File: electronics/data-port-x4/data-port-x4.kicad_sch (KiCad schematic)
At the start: 0 parts

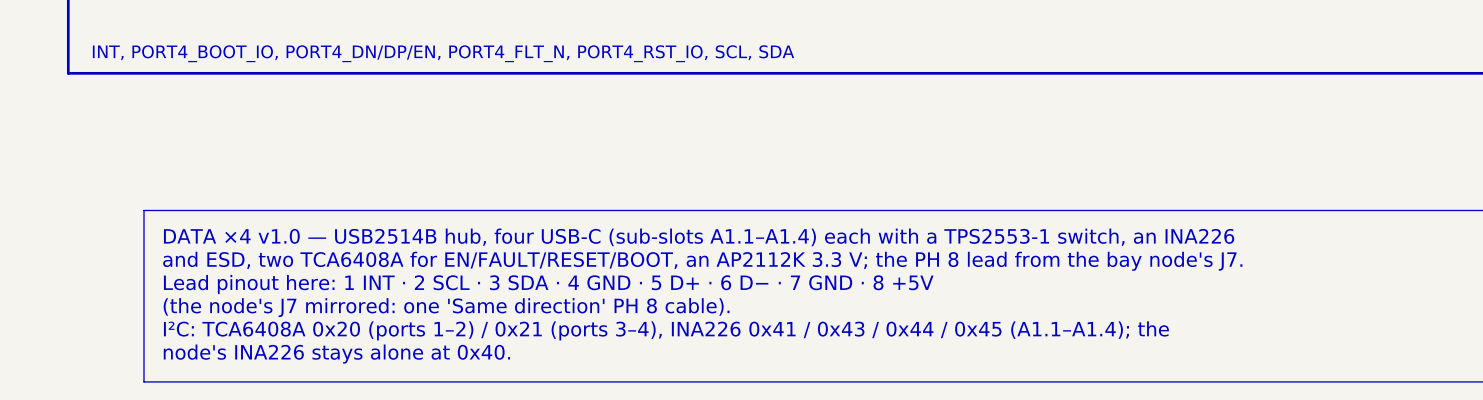
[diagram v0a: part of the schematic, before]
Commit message: DATA ×4: the lead's D+/D− follow J7, the upstream pair rerouted
The node's J7 now has D+ on pin 3 and D− on pin 4 (094341c); the lead
mirrors pins (n ↔ 9 − n), so J1 takes D− on pin 5 and D+ on pin 6, like
the single DATA port's J2.  The upstream pair is drawn again without a
crossover: two vias in front of J1 (D+ north of D−), B.Cu west, north
along x 87 (clear of In2's +3V3 edge), west and south into the hub's top
pins; every turn keeps D+ on the pair's right, west of D− at the hub.

The new route moved the router's vias, and two of them cut In2's +5V in
half under the hub's capacitors: the +3V3 tab there ends at y 21.6 and a
via-only keep-out (pcbgen keepouts "vias_only") keeps the 1.9 mm +5V neck
whole.  The 22 µF VBUS caps' LCSC/MPN fields now reach the schematic and
the PCB too.  Docs: the lead pinout row.

ERC 0, DRC 0 (unconnected 0, parity 0); Konnect: 0 errors, the same three
library-copy warnings, JLC DFM 0.

Co-Authored-By: Claude Opus 5.5 <noreply@anthropic.com>
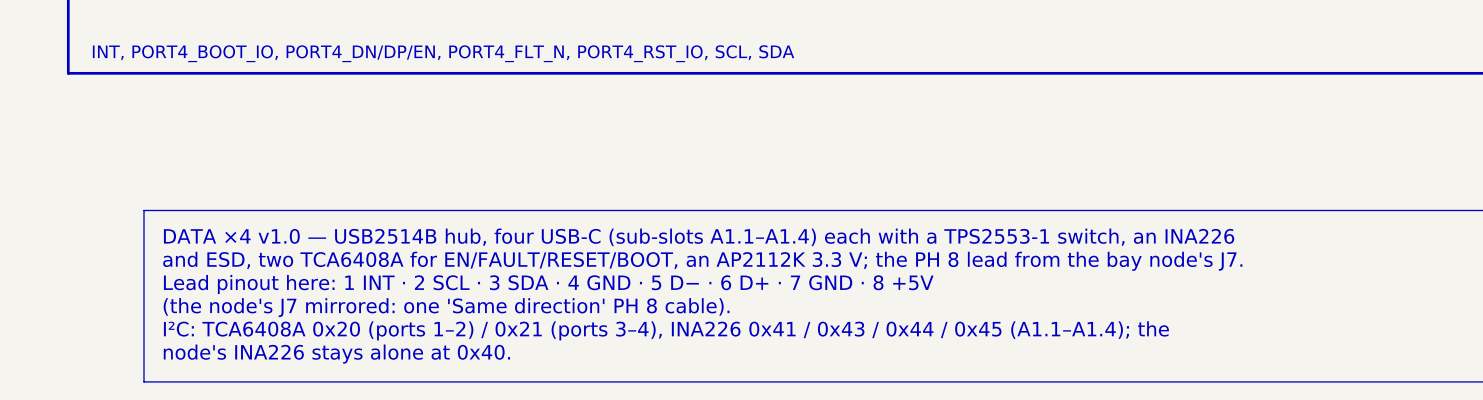
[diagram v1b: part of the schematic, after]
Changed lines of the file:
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@@
 		)
 	)
-	(text_box "DATA ×4 v1.0 — USB2514B hub, four USB-C (sub-slots A1.1–A1.4) each with a TPS2553-1 switch, an INA226\n  and ESD, two TCA6408A for EN/FAULT/RESET/BOOT, an AP2112K 3.3 V; the PH 8 lead from the bay node's J7.\nLead pinout here: 1 INT · 2 SCL · 3 SDA · 4 GND · 5 D+ · 6 D− · 7 GND · 8 +5V\n  (the node's J7 mirrored: one 'Same direction' PH 8 cable).\nI²C: TCA6408A 0x20 (ports 1–2) / 0x21 (ports 3–4), INA226 0x41 / 0x43 / 0x44 / 0x45 (A1.1–A1.4); the\n  node's INA226 stays alone at 0x40."
+	(text_box "DATA ×4 v1.0 — USB2514B hub, four USB-C (sub-slots A1.1–A1.4) each with a TPS2553-1 switch, an INA226\n  and ESD, two TCA6408A for EN/FAULT/RESET/BOOT, an AP2112K 3.3 V; the PH 8 lead from the bay node's J7.\nLead pinout here: 1 INT · 2 SCL · 3 SDA · 4 GND · 5 D− · 6 D+ · 7 GND · 8 +5V\n  (the node's J7 mirrored: one 'Same direction' PH 8 cable).\nI²C: TCA6408A 0x20 (ports 1–2) / 0x21 (ports 3–4), INA226 0x41 / 0x43 / 0x44 / 0x45 (A1.1–A1.4); the\n  node's INA226 stays alone at 0x40."
 		(exclude_from_sim no)
 		(at 30 219.71 0)

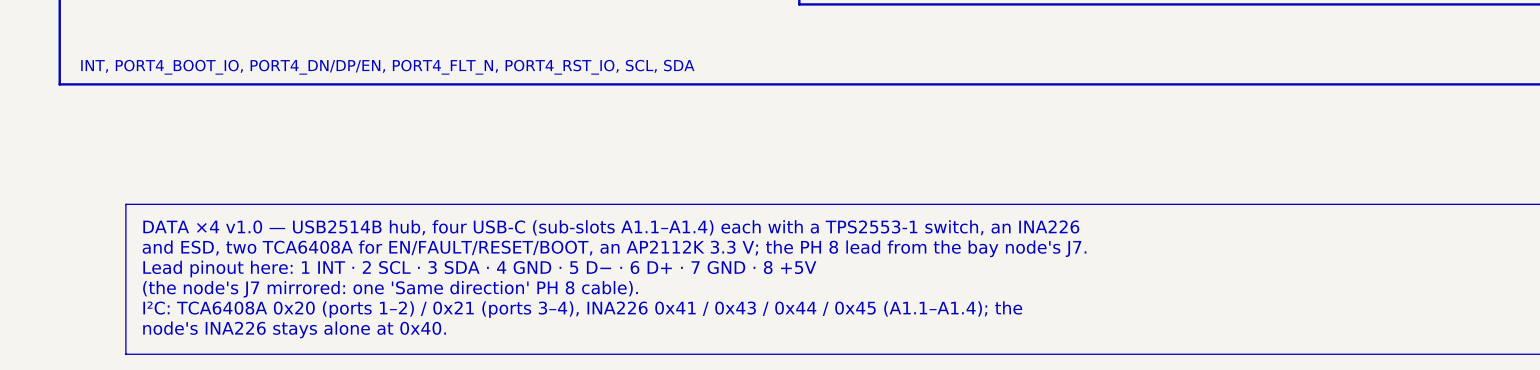
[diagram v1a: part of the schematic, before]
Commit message: DATA ×4: a basic-part LDO, the XC6206 in U3's spot
U3 goes from the AP2112K-3.3 (extended) to the XC6206P332MR-G (C5446,
JLC basic, SOT-23-3): one extended part type fewer, $3.07 an order at
Economic PCBA.  Its dropout is ≈ 0.25 V at 0.1 A against the board's
≈ 0.1 A of logic, so the hub, the expanders and the INA226s still run
down to ≈ 3.6 V in; 200 mA max, 6 V in max (the node's +5V is 5.24 V).
The AMS1117 suggested first doesn't fit (SOT-223 under J1) and its ≈ 1 V
dropout would eat the lead's margin.  U3 sits at 0° (of three
orientations routed, the one Freerouting closed), CPL fix 180° for
C5446.

Re-routed: ERC 0, DRC 0 (unconnected 0, parity 0).  BOM: the DATA ×4
quote at 8 extended types ($74.44), its lever moves out of JLC_LEVERS.

Co-Authored-By: Claude Opus 5.5 <noreply@anthropic.com>
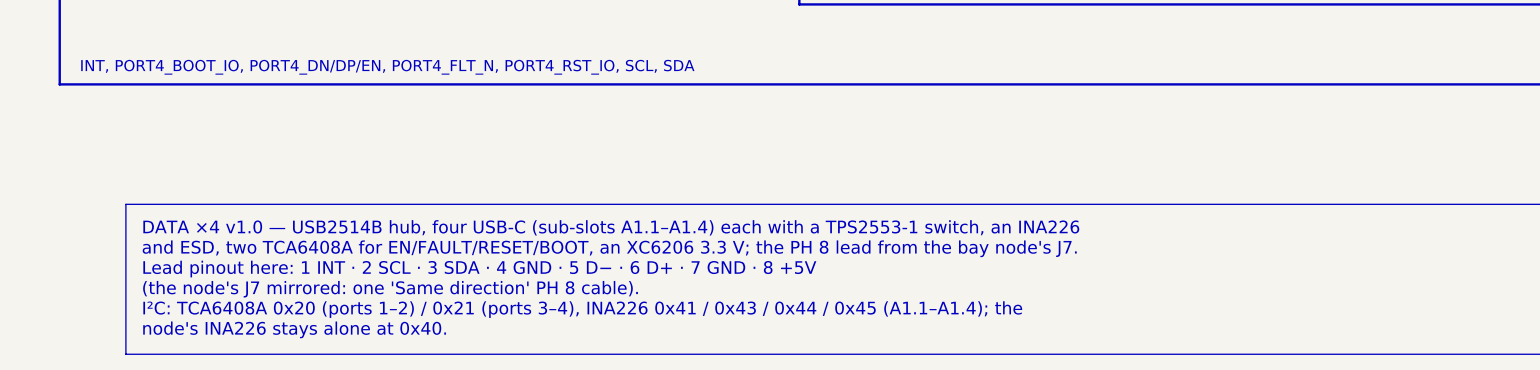
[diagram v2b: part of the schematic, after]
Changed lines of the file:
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@@
 		)
 	)
-	(text_box "DATA ×4 v1.0 — USB2514B hub, four USB-C (sub-slots A1.1–A1.4) each with a TPS2553-1 switch, an INA226\n  and ESD, two TCA6408A for EN/FAULT/RESET/BOOT, an AP2112K 3.3 V; the PH 8 lead from the bay node's J7.\nLead pinout here: 1 INT · 2 SCL · 3 SDA · 4 GND · 5 D− · 6 D+ · 7 GND · 8 +5V\n  (the node's J7 mirrored: one 'Same direction' PH 8 cable).\nI²C: TCA6408A 0x20 (ports 1–2) / 0x21 (ports 3–4), INA226 0x41 / 0x43 / 0x44 / 0x45 (A1.1–A1.4); the\n  node's INA226 stays alone at 0x40."
+	(text_box "DATA ×4 v1.0 — USB2514B hub, four USB-C (sub-slots A1.1–A1.4) each with a TPS2553-1 switch, an INA226\n  and ESD, two TCA6408A for EN/FAULT/RESET/BOOT, an XC6206 3.3 V; the PH 8 lead from the bay node's J7.\nLead pinout here: 1 INT · 2 SCL · 3 SDA · 4 GND · 5 D− · 6 D+ · 7 GND · 8 +5V\n  (the node's J7 mirrored: one 'Same direction' PH 8 cable).\nI²C: TCA6408A 0x20 (ports 1–2) / 0x21 (ports 3–4), INA226 0x41 / 0x43 / 0x44 / 0x45 (A1.1–A1.4); the\n  node's INA226 stays alone at 0x40."
 		(exclude_from_sim no)
 		(at 30 219.71 0)

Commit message: DATA ×4: back to the AP2112K on U3, on top-side copper
The XC6206 (82c7172) can't carry this rail.  The USB2514B alone draws up
to 155 mA at high speed with four ports busy (datasheet tables 6-4 and
6-5; 84 mA at full speed), so the LDO burns ≈ 0.31 W from 5.24 V: more
than a 200 mA SOT-23 LDO like the XC6206 is rated for (≈ 0.25 W), and the
XC6206 has no thermal shutdown.  The AP2112K-3.3 (600 mA, thermal
shutdown) is back on its SOT-23-5 footprint at 0°, CPL 270° as before;
C5446 and its catalog entry go.

Its VIN and EN pins (with C2's +5V pad) and its GND pin now sit on
top-side islands (exclusive, thermal reliefs) with their own vias to the
+5V and GND planes, to spread that heat.  design.py and docs/electronics.md
say why, so it isn't swapped again.

Re-routed: ERC 0, DRC 0 (unconnected 0, parity 0).  BOM: back to 9
extended types, the DATA ×4 order $103.76.

Co-Authored-By: Claude Opus 5.5 <noreply@anthropic.com>
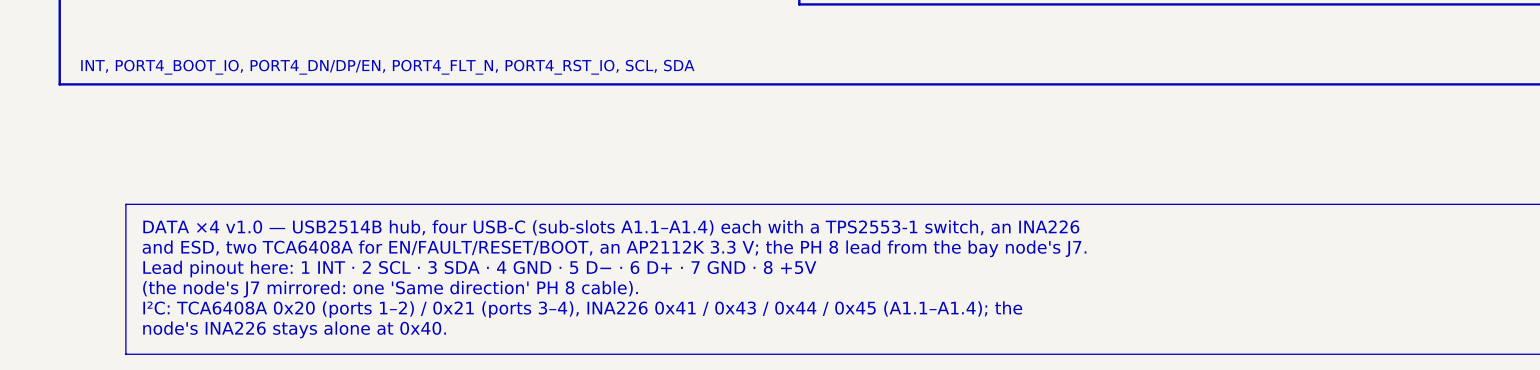
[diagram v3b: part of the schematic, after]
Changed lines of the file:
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@@
 		)
 	)
-	(text_box "DATA ×4 v1.0 — USB2514B hub, four USB-C (sub-slots A1.1–A1.4) each with a TPS2553-1 switch, an INA226\n  and ESD, two TCA6408A for EN/FAULT/RESET/BOOT, an XC6206 3.3 V; the PH 8 lead from the bay node's J7.\nLead pinout here: 1 INT · 2 SCL · 3 SDA · 4 GND · 5 D− · 6 D+ · 7 GND · 8 +5V\n  (the node's J7 mirrored: one 'Same direction' PH 8 cable).\nI²C: TCA6408A 0x20 (ports 1–2) / 0x21 (ports 3–4), INA226 0x41 / 0x43 / 0x44 / 0x45 (A1.1–A1.4); the\n  node's INA226 stays alone at 0x40."
+	(text_box "DATA ×4 v1.0 — USB2514B hub, four USB-C (sub-slots A1.1–A1.4) each with a TPS2553-1 switch, an INA226\n  and ESD, two TCA6408A for EN/FAULT/RESET/BOOT, an AP2112K 3.3 V; the PH 8 lead from the bay node's J7.\nLead pinout here: 1 INT · 2 SCL · 3 SDA · 4 GND · 5 D− · 6 D+ · 7 GND · 8 +5V\n  (the node's J7 mirrored: one 'Same direction' PH 8 cable).\nI²C: TCA6408A 0x20 (ports 1–2) / 0x21 (ports 3–4), INA226 0x41 / 0x43 / 0x44 / 0x45 (A1.1–A1.4); the\n  node's INA226 stays alone at 0x40."
 		(exclude_from_sim no)
 		(at 30 219.71 0)

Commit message: DATA ×4: 100 × 28 mm, the lead on the right edge
The board shrinks to 100 mm (JLC's 4-layer offer, no engineering fee)
and grows 4 mm towards the rear: 100 × 28, no notch.  The four USB-C,
their ports, pairs and ESD flow-through stay exactly where they were
(the layout moves 4 mm off the rear edge as a whole, DY in design.py).
J1 (PH 8, side entry) moves to the right edge, its mouth at drawer x 115,
pin 1 at the front; its lead ESDs face its pins, U4 turned 270°, U5 level
with pin 1; C1 by its +5V pin; U3 behind it, turned 180° with its VIN,
EN and GND islands (the same shapes) and a +3V3 bump in In2 under its
output.  H1-H3 keep their drawer spots, H4 moves to the rear-right corner
(96.8, 3.5): the drawer's one set of DATA ×4 bosses, the v2's too.

Routing against the 108 mm board: the upstream pair goes from 26 / 25 mm
to 15 / 15 mm, two vias each as before; the 16 port pair nets are
unchanged to 0.05 mm and to the via; no B.Cu pair segment over In2's
+3V3 (both notches kept); the +5V neck under the hub stays 2.44 mm with
no via; the LDO islands are as large (EN 4.7 mm² against 4.4).  Router
copper 721 mm and 91 vias against 799 mm and 93.  Port 3's INA226 A1
strap gets a via of its own (its fan-out had no room, Freerouting missed
it now and then).  Nothing ends up worse.

ERC 0, DRC 0, parity 0, 0 unconnected (the best of seven routing
variants on the Mac and zephyrbox).  The review's CPL audit agrees on all
106 parts.  rack.yaml carries the new size, holes and J1 (`lead`, the
notch and `ph` gone); the viewer's stand-in shows J1 on the right edge
and brings the lead up beside the board.  The bare PCB is priced at the
bay node's 4-layer offer ($13.20 for 5) until the JLC-cost owner
re-quotes it: about $85 for 5 with 2 assembled instead of $104.  The
drawer's window and the new H4 boss are the Mechanics session's.

Co-Authored-By: Claude Opus 5.5 <noreply@anthropic.com>
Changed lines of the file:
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@@
 		)
 	)
-	(text_box "DATA ×4 v1.0 — USB2514B hub, four USB-C (sub-slots A1.1–A1.4) each with a TPS2553-1 switch, an INA226\n  and ESD, two TCA6408A for EN/FAULT/RESET/BOOT, an AP2112K 3.3 V; the PH 8 lead from the bay node's J7.\nLead pinout here: 1 INT · 2 SCL · 3 SDA · 4 GND · 5 D− · 6 D+ · 7 GND · 8 +5V\n  (the node's J7 mirrored: one 'Same direction' PH 8 cable).\nI²C: TCA6408A 0x20 (ports 1–2) / 0x21 (ports 3–4), INA226 0x41 / 0x43 / 0x44 / 0x45 (A1.1–A1.4); the\n  node's INA226 stays alone at 0x40."
+	(text_box "DATA ×4 v1.0 — USB2514B hub, four USB-C (sub-slots A1.1–A1.4) each with a TPS2553-1 switch, an INA226\n  and ESD, two TCA6408A for EN/FAULT/RESET/BOOT, an AP2112K 3.3 V; the PH 8 lead from the bay node's J7\n  into J1 on the right edge.  100 × 28 mm.\nLead pinout here: 1 INT · 2 SCL · 3 SDA · 4 GND · 5 D− · 6 D+ · 7 GND · 8 +5V\n  (the node's J7 mirrored: one 'Same direction' PH 8 cable).\nI²C: TCA6408A 0x20 (ports 1–2) / 0x21 (ports 3–4), INA226 0x41 / 0x43 / 0x44 / 0x45 (A1.1–A1.4); the\n  node's INA226 stays alone at 0x40."
 		(exclude_from_sim no)
 		(at 30 219.71 0)
-		(size 360 19.05)
+		(size 360 21.59)
 		(margins 2 2 2 2)
 		(stroke

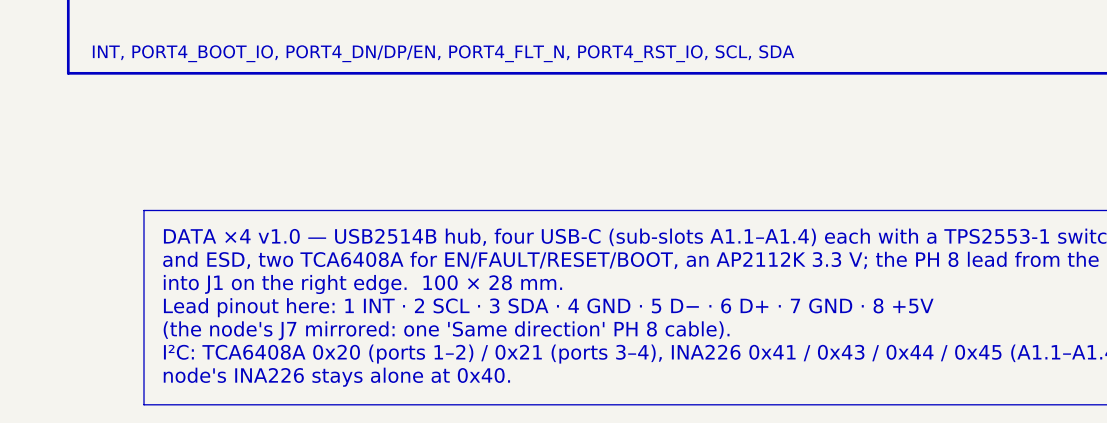
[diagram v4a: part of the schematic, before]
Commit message: DATA ×4: 100 × 37 mm, J1 at the rear end of the right edge, no fourth hole
On top of 1c0dfbd (100 × 28, J1 centred on the right edge):
- 100 × 37 mm, as deep as the v2: 13 mm deeper than the layout's 24 mm frame, still under JLC's 100 mm
  4-layer offer.
- J1 at the rear end of the right edge: mouth at drawer x 115, pins at drawer y 176–190, the plug
  (y ≈ 174–192) over the drawer's side window and clear of the v2's front-right boss. The LDO block
  and its islands sit in the corner behind it, unchanged.
- No fourth hole: v1 sits on H1–H3, unchanged in drawer coordinates, and on the front ledges. The
  plug forces stay in the board's plane. The drawer (2a3309b) already has no boss there.
- The upstream pair runs 45° from J1's vias into the hub's notch, and In2's +3V3 edge follows the
  diagonal: 16.7 / 17.2 mm pad to pin, 2 vias (1c0dfbd: 14.7 / 14.5). The lead's ESDs line up with
  J1's pins (flow-through). C13 and R2 move north of R5.

Against 1c0dfbd, unchanged or better:
- port pairs, their ESDs and the B.Cu lanes unchanged;
- every pair on one reference plane end to end (+5V on In2);
- +5V neck 2.45 mm (2.34);
- LDO islands unchanged (1.31 / 1.31 / 4.72 mm²);
- router copper 1580 mm (1612), signal vias 76 (79): the best of seven Freerouting variants. The 59
  extra GND vias are the larger pours' stitching.
- ERC 0, DRC 0, parity 0, 0 unconnected.
- CPL audit: 99 parts pass. The flags are the same 7 as 1c0dfbd's, positions agree: the USB4105s'
  symmetric pin 1, and the C1 / J1 / U3 land residuals against EasyEDA.

Worse:
- the upstream pair is 2.0 / 2.7 mm longer. J1's pins moved 6.4 mm to the rear, and a 45° route
  cannot do better (≈ 15 ps at 480 Mb/s, beside a 45 cm lead).
- its D+/D− mismatch is 0.53 mm (0.23). That is under the 1.27 mm usual for USB 2.0, and the
  downstream pairs already differ by 2.2 mm.

JLC's bare PCB at 100 × 37 (calculator, 2026-10-20): $13.10 for 5 ($8.00 offer + lead-free HASL
$5.10, no deburring line), $19.20 / $53.80 / $73.40 f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
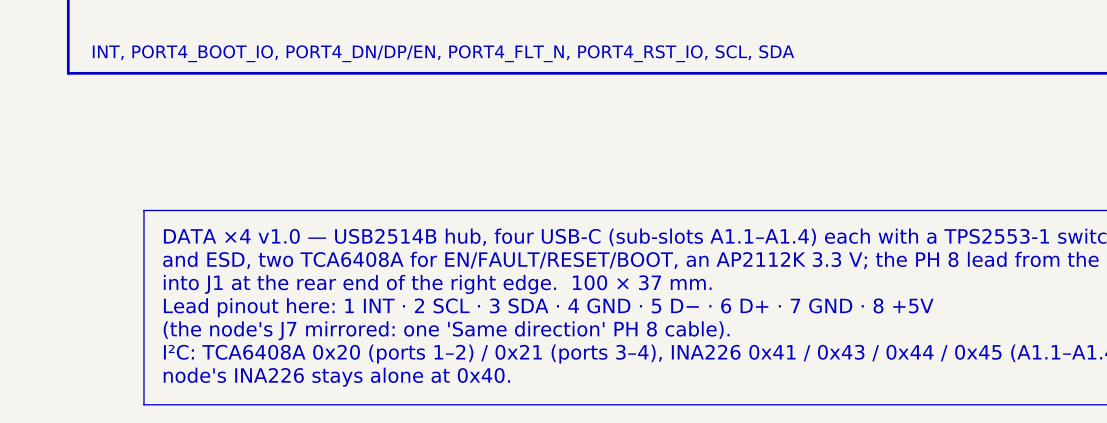
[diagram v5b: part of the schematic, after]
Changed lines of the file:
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@@
 		)
 	)
-	(text_box "DATA ×4 v1.0 — USB2514B hub, four USB-C (sub-slots A1.1–A1.4) each with a TPS2553-1 switch, an INA226\n  and ESD, two TCA6408A for EN/FAULT/RESET/BOOT, an AP2112K 3.3 V; the PH 8 lead from the bay node's J7\n  into J1 on the right edge.  100 × 28 mm.\nLead pinout here: 1 INT · 2 SCL · 3 SDA · 4 GND · 5 D− · 6 D+ · 7 GND · 8 +5V\n  (the node's J7 mirrored: one 'Same direction' PH 8 cable).\nI²C: TCA6408A 0x20 (ports 1–2) / 0x21 (ports 3–4), INA226 0x41 / 0x43 / 0x44 / 0x45 (A1.1–A1.4); the\n  node's INA226 stays alone at 0x40."
+	(text_box "DATA ×4 v1.0 — USB2514B hub, four USB-C (sub-slots A1.1–A1.4) each with a TPS2553-1 switch, an INA226\n  and ESD, two TCA6408A for EN/FAULT/RESET/BOOT, an AP2112K 3.3 V; the PH 8 lead from the bay node's J7\n  into J1 at the rear end of the right edge.  100 × 37 mm.\nLead pinout here: 1 INT · 2 SCL · 3 SDA · 4 GND · 5 D− · 6 D+ · 7 GND · 8 +5V\n  (the node's J7 mirrored: one 'Same direction' PH 8 cable).\nI²C: TCA6408A 0x20 (ports 1–2) / 0x21 (ports 3–4), INA226 0x41 / 0x43 / 0x44 / 0x45 (A1.1–A1.4); the\n  node's INA226 stays alone at 0x40."
 		(exclude_from_sim no)
 		(at 30 219.71 0)
